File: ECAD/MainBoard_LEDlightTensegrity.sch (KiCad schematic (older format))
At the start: 3 parts, among them IC1 ARDUINO_PRO_MINI_5V, U1 REDBOTACCEL

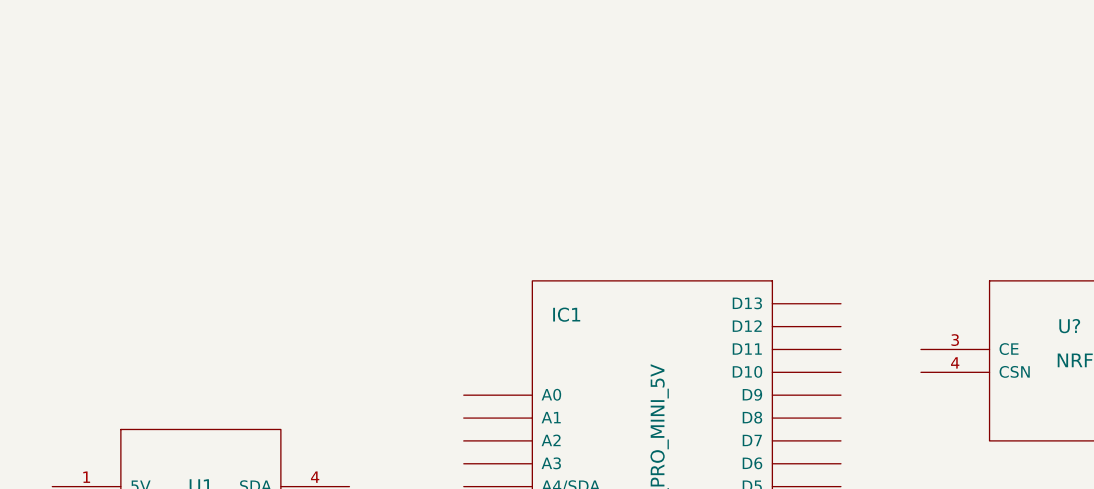
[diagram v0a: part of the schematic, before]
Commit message: added LDO to schematic and made library component
Added CJ1117-3.3 LDO from SeeedStudio's Open Parts Library
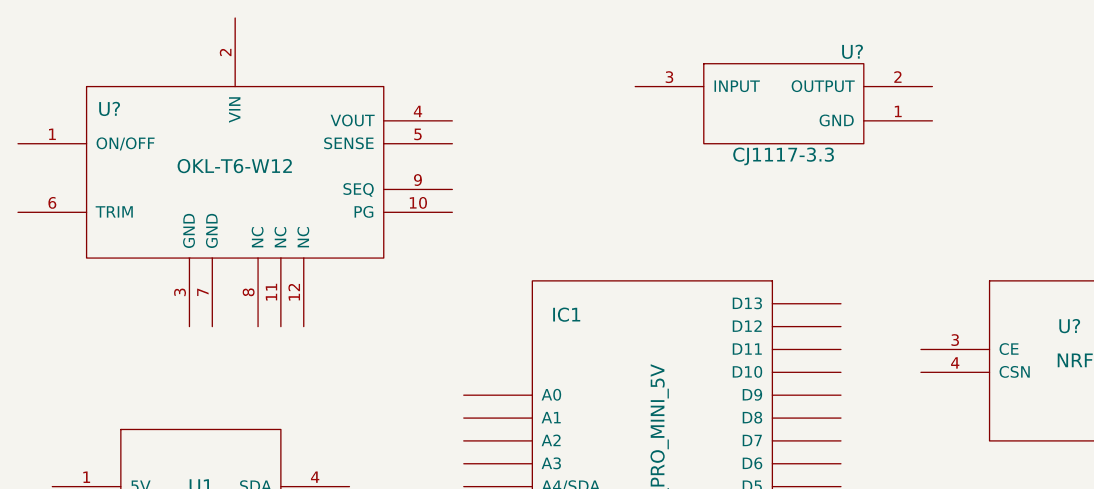
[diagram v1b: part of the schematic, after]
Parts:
- added U?: OKL-T6-W12, symbol OKL-T6-W12
- added U?: CJ1117-3.3, symbol CJ1117-3.3
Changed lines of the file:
@@
 Sheet 1 1
 Title ""
-Date "28 aug 2014"
+Date "29 aug 2014"
 Rev ""
 Comp ""
@@
 	1    0    0    -1
 $EndComp
+$Comp
+L OKL-T6-W12 U?
+U 1 1 53FE95D6
+P 3600 2200
+F 0 "U?" H 3050 2450 60  0000 C CNN
+F 1 "OKL-T6-W12" H 3600 2200 60  0000 C CNN
+F 2 "" H 3650 2350 60  0000 C CNN
+F 3 "" H 3650 2350 60  0000 C CNN
+	1    3600 2200
+	1    0    0    -1
+$EndComp
+$Comp
+L CJ1117-3.3 U?
+U 1 1 54001795
+P 6000 1950
+F 0 "U?" H 6300 2200 60  0000 C CNN
+F 1 "CJ1117-3.3" H 6000 1750 60  0000 C CNN
+F 2 "" H 6000 1950 60  0000 C CNN
+F 3 "" H 6000 1950 60  0000 C CNN
+	1    6000 1950
+	1    0    0    -1
+$EndComp

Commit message: First Version of Schematic Complete
Generated Netlist
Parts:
- added K1, K2, K3: CONN_3, symbol CONN_3
- added P1: CONN_2, symbol CONN_2
- added R1: 1.33K, ~, symbol R
- added R2: 300, ~, symbol R
- added R? (x2): 0, ~, symbol R
- added SW1: SPST, ~, symbol SPST
- gave numbers to parts that had none: 3
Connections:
- net SDA: now reaches IC1.~ (VCC)
- net SDA: now also U1.4 (SDA)
- net +5V: now reaches U1.1 (5V)
- net +5V: now also U2.4 (VOUT), U2.5 (SENSE), U3.3 (INPUT), K3.2 (PM), R?.1, R?.1
- net GND: now reaches U1.2 (GND)
- net GND: now also IC1.~ (VCC), U2.3 (GND), U2.7 (GND), U3.1 (GND), U4.1 (GND), K3.3 (P3), R1.2, SW1.1
- net SCL: now reaches U1.3 (SCL)
- net SCL: now also IC1.~ (VCC)
- net at U4.2 (3.3V): now also U3.2 (OUTPUT)
- net CE: now reaches U4.3 (CE)
- net CE: now also IC1.~ (VCC)
- net CSN: now reaches U4.4 (CSN)
- net CSN: now also IC1.~ (VCC)
- net SCK: now reaches U4.5 (SCK)
- net SCK: now also IC1.~ (VCC)
- net MOSI: now reaches U4.6 (MOSI)
- net MOSI: now also IC1.~ (VCC)
- net MISO: now reaches U4.7 (MISO)
- net MISO: now also IC1.~ (VCC)
- net at U2.1 (ON/OFF): now also SW1.2
- net at U2.10 (PG): now also P1.2 (PM)
- net VCC: now reaches U2.2 (VIN)
- net at U2.6 (TRIM): now also R1.1
- net at U2.9 (SEQ): now also P1.1 (P1)
- new net: IC1.~ (VCC), K1.1 (P1)
- new net: IC1.~ (VCC), K1.2 (PM)
- new net: IC1.~ (VCC), K1.3 (P3)
- new net: IC1.~ (VCC), K2.1 (P1)
- new net: IC1.~ (VCC), K2.2 (PM)
- new net: IC1.~ (VCC), K2.3 (P3)
- new net: IC1.~ (VCC), R2.1
- new net: IC1.~ (VCC), R?.2 (x2)
- new net LED: K3.1 (P1), R2.2
- no-connect marks 0 -> 21
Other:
- moved on the sheet: IC1, U1, U2, U3, U4
